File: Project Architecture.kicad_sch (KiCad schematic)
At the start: 0 parts

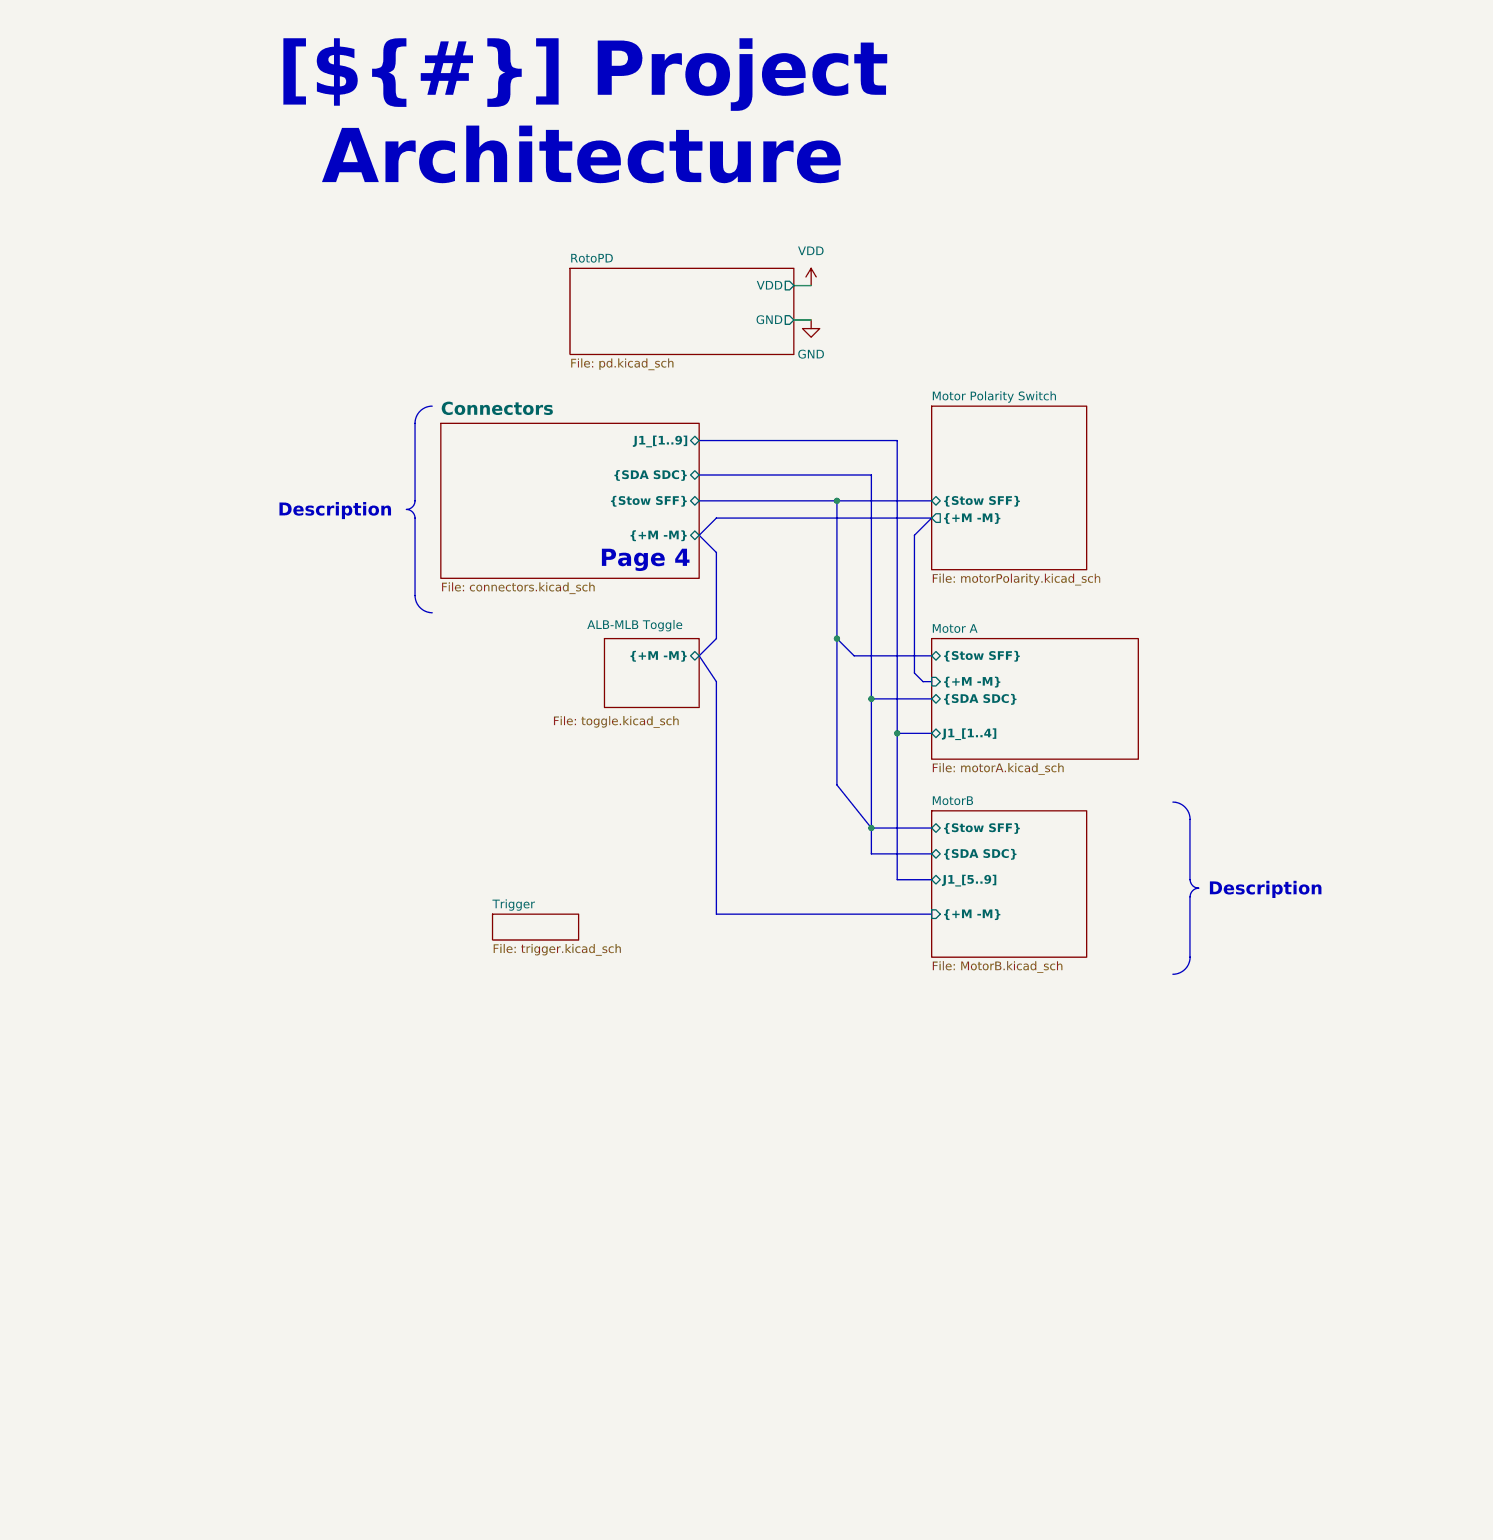
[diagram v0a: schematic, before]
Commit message: updated architecture page
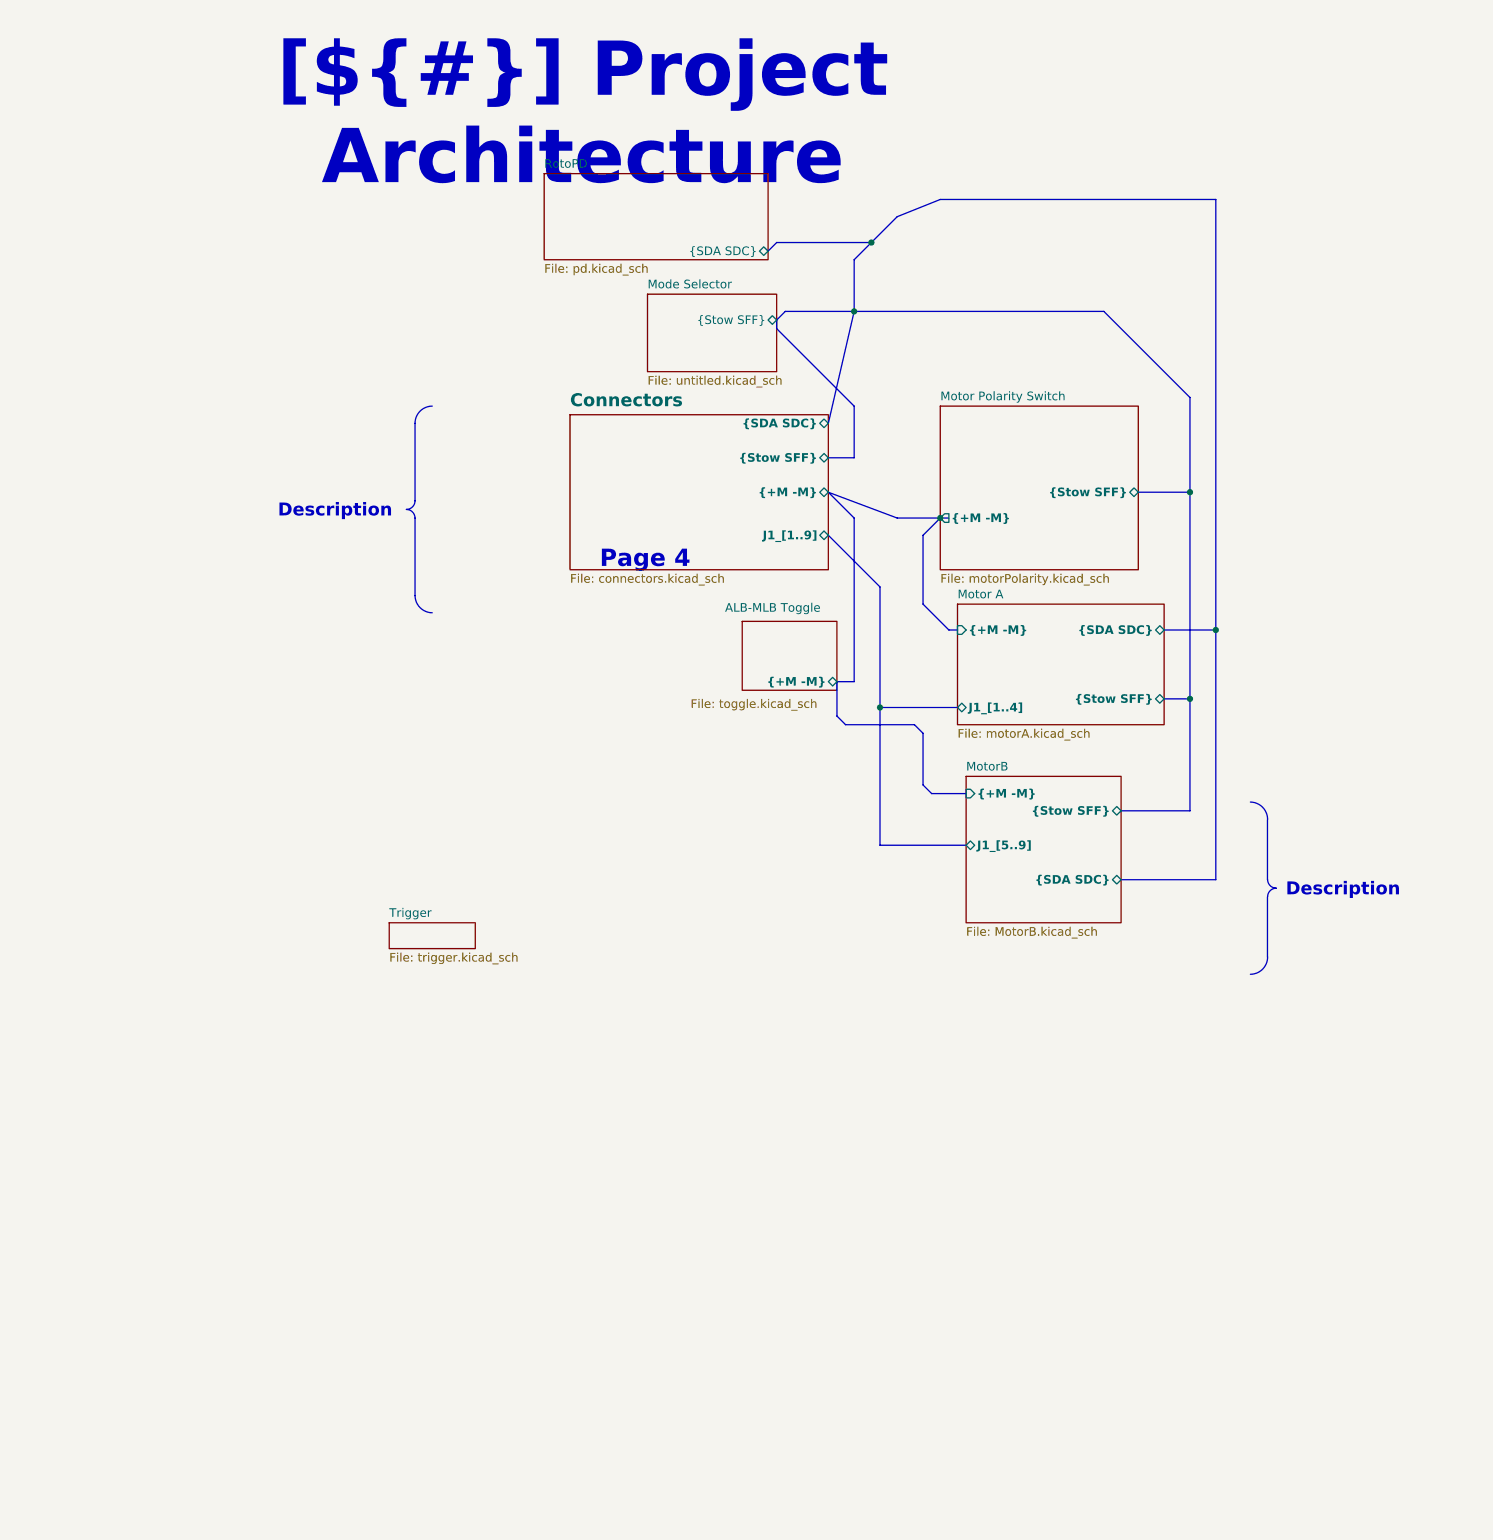
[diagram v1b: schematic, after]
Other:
- added sheet Mode Selector (untitled.kicad_sch)
- sheet RotoPD ports: added {SDA SDC}; removed GND, VDD

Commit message: begin pcb
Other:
- added sheet AlbMlb test harnes (testhatness.kicad_sch)
- added sheet Raspberrypi (pi.kicad_sch)
- added sheet encoders (encoders.kicad_sch)
- sheet ALB-MLB Toggle ports: added {+MB -MB}; removed none
- sheet Connectors ports: added RE1{+3.3V A B C}, RE2{GND A B C }, Trigger, {+MB -MB}; removed none
- sheet MotorB ports: added {+MB -MB}; removed {+M -M}
- sheet Trigger ports: added PWM, Trigger, {+M}; removed none
- note removed: "Page 4"
